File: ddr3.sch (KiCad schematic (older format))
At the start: 35 parts, among them U12 TPS51200DRC, U13 AS4C256M16D3

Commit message: DDR3 sheet edits
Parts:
- removed R51, R52: 51, Resistor_SMD:R_0402_1005Metric, symbol Device:R_Small
- removed U12: TPS51200DRC, Package_SON:VSON-10-1EP_3x3mm_P0.5mm_EP1.65x2.4mm, symbol Regulator_Linear:TPS51200DRC
- removed U13: AS4C256M16D3, Package_BGA:BGA-96_9.0x13.0mm_Layout2x3x16_P0.8mm, symbol eco_memory:AS4C256M16D3
- added R? (x2): R_51R_0402, antmicro-footprints:0402-res, symbol antmicroResistors0402:R_51R_0402
- added U? (x2): AS4C256M16D3, antmicro-footprints:BGA-96_9.0x13.0mm_Layout2x3x16_P0.8mm, symbol antmicroMemory:AS4C256M16D3
- added U?: TPS51200DRC, antmicro-footprints:VSON-10-1EP_3x3mm, symbol antmicroPMICVoltageRegulatorsDCDCSwitchingControllers:TPS51200DRC
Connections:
- net labels added: DDR3_VREF, DDR3_VTT_EN
- net labels removed: DDR3_Vref, DDR3_Vtt_EN, VO
- wire segments 334 -> 329
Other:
- note removed: "TODO:Replace 51R resistors"
- moved on the sheet: C?, R?

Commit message: Initial component placement added (to be adjusted further)
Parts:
- gave numbers to parts that had none: 35

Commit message: Update after designator unification
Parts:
- renumbered C123 to C40, C124 to C41, C125 to C42, C126 to C43, C127 to C44, C131 to C45, C132 to C46, C133 to C47, C134 to C48, C135 to C49, C137 to C50, C142 to C51, C146 to C52, C150 to C53, C154 to C54, C157 to C55, C158 to C56, C159 to C57, C160 to C58, C161 to C59, C162 to C60, C163 to C61, C164 to C62, C165 to C63, R56 to R54, R57 to R55, R58 to R56, R59 to R57, R60 to R58, R61 to R59, R62 to R60, R63 to R61, R64 to R62, U13 to U7, U14 to U8

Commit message: Add local component libraries
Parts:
- removed R61, R62: R_51R_0402, antmicro-footprints:0402-res, symbol antmicroResistors0402:R_51R_0402
- added R? (x2): R_51R_0402, antmicro-footprints:0402-res, symbol antmicroResistors0402:R_51R_0402
- C40, C41, C43, C47: footprint antmicro-footprints:0402-cap -> artix-dc-scm-footprints:0402-cap; symbol antmicroCapacitors0402:C_10u_0402 -> artix-dc-scm:C_10u_0402
- C42, C44, C45, C46, C57, C62, C63: footprint antmicro-footprints:0402-cap -> artix-dc-scm-footprints:0402-cap; symbol antmicroCapacitors0402:C_100n_0402 -> artix-dc-scm:C_100n_0402
- C48: footprint antmicro-footprints:0402-cap -> artix-dc-scm-footprints:0402-cap; symbol antmicroCapacitors0402:C_4u7_0402 -> artix-dc-scm:C_4u7_0402
- C49, C50, C51, C52, C53, C54, C55, C56, C58, C59, C60, C61: footprint antmicro-footprints:0402-cap -> artix-dc-scm-footprints:0402-cap; symbol antmicroCapacitors0402:C_470n_0402 -> artix-dc-scm:C_470n_0402
- R54, R55, R56: footprint antmicro-footprints:R_Array_Convex_8x0602 -> artix-dc-scm-footprints:R_Array_Convex_8x0602; symbol antmicroResistorNetworksArrays:8x51R_0602_array -> artix-dc-scm:8x51R_0602_array
- R57, R58, R59: footprint antmicro-footprints:0402-res -> artix-dc-scm-footprints:0402-res; symbol antmicroResistors0402:R_10k_0402 -> artix-dc-scm:R_10k_0402
- R60: footprint antmicro-footprints:0402-res -> artix-dc-scm-footprints:0402-res; symbol antmicroResistors0402:R_240R_0402 -> artix-dc-scm:R_240R_0402
- U7: footprint antmicro-footprints:BGA-96_9.0x13.0mm_Layout2x3x16_P0.8mm -> artix-dc-scm-footprints:BGA-96_9.0x13.0mm_Layout2x3x16_P0.8mm; symbol antmicroMemory:AS4C256M16D3 -> artix-dc-scm:AS4C256M16D3
- U8: footprint antmicro-footprints:VSON-10-1EP_3x3mm -> artix-dc-scm-footprints:VSON-10-1EP_3x3mm; symbol antmicroPMICVoltageRegulatorsDCDCSwitchingControllers:TPS51200DRC -> artix-dc-scm:TPS51200DRC

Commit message: Component placement done
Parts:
- R100, R99: renamed from R?; footprint antmicro-footprints:0402-res -> artix-dc-scm-footprints:0402-res; symbol antmicroResistors0402:R_51R_0402 -> artix-dc-scm:R_51R_0402
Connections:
- net DDR3_CLK+: now also R99.2; no longer R99.1
- net at C63.2, R100.1: now also R99.1; no longer R99.2
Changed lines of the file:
@@
 DDR3_VTT
 $Comp
-L antmicroResistors0402:R_51R_0402 R?
+L artix-dc-scm:R_51R_0402 R99
 U 1 1 5FDBE47E
 P 12475 8050
-F 0 "R?" V 12430 8120 60  0000 L CNN
+F 0 "R99" V 12430 8120 60  0000 L CNN
 F 1 "R_51R_0402" H 12475 7900 60  0001 C CNN
-F 2 "antmicro-footprints:0402-res" H 12675 8250 60  0001 L CNN
+F 2 "artix-dc-scm-footprints:0402-res" H 12675 8250 60  0001 L CNN
 F 3 "" H 12475 8050 50  0001 C CNN
 F 4 "YAGEO" H 12675 8450 60  0001 L CNN "Manufacturer"
@@
 F 6 "51R" V 12528 8120 50  0000 L CNN "Val"
 	1    12475 8050
-	0    1    1    0
+	0    1    -1   0
 $EndComp
 $Comp
-L antmicroResistors0402:R_51R_0402 R?
+L artix-dc-scm:R_51R_0402 R100
 U 1 1 5FDBF551
 P 12475 8450
-F 0 "R?" V 12430 8520 60  0000 L CNN
+F 0 "R100" V 12430 8520 60  0000 L CNN
 F 1 "R_51R_0402" H 12475 8300 60  0001 C CNN
-F 2 "antmicro-footprints:0402-res" H 12675 8650 60  0001 L CNN
+F 2 "artix-dc-scm-footprints:0402-res" H 12675 8650 60  0001 L CNN
 F 3 "" H 12475 8450 50  0001 C CNN
 F 4 "YAGEO" H 12675 8850 60  0001 L CNN "Manufacturer"

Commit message: Improved DDR3 related connection (WIP)
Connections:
- net DDR3_A0: now also R54.5; no longer R55.8
- net DDR3_A1: now also R55.7; no longer R55.2
- net DDR3_A10: now also R54.1; no longer R55.5
- net DDR3_A11: now also R55.8; no longer R54.8
- net DDR3_A12: now also R55.4; no longer R55.3
- net DDR3_A13: now also R54.8; no longer R54.1
- net DDR3_A14: now also R54.2; no longer R54.7
- net DDR3_A2: now also R54.6; no longer R54.4
- net DDR3_A3: now also R56.4; no longer R56.2
- net DDR3_A4: now also R55.3; no longer R55.1
- net DDR3_A5: now also R56.3; no longer R56.1
- net DDR3_A6: now also R55.5; no longer R54.5
- net DDR3_A7: now also R56.2; no longer R54.3
- net DDR3_A8: now also R55.6; no longer R54.6
- net DDR3_A9: now also R54.7; no longer R54.2
- net DDR3_BA0: now also R56.5; no longer R56.3
- net DDR3_BA1: now also R55.2; no longer R55.4
- net DDR3_BA2: now also R54.4; no longer R55.7
- net DDR3_CAS: now also R56.6; no longer R56.8
- net DDR3_CKE: now also R55.1; no longer R56.7
- net DDR3_CS: now also R56.7; no longer R56.4
- net DDR3_ODT: now also R56.8; no longer R56.6
- net DDR3_RAS: now also R56.1; no longer R56.5
- net DDR3_WE: now also R54.3; no longer R55.6
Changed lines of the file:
@@
 Wire Wire Line
 	11775 2375 11775 2700
+Text GLabel 4425 9375 0    50   UnSpc ~ 0
+DDR3_A1
+Text GLabel 4425 8975 0    50   UnSpc ~ 0
+DDR3_A4
+Text GLabel 4425 9175 0    50   UnSpc ~ 0
+DDR3_A6
+Text GLabel 4425 9275 0    50   UnSpc ~ 0
+DDR3_A8
 Text GLabel 4425 9475 0    50   UnSpc ~ 0
-DDR3_A0
+DDR3_A11
+Text GLabel 4425 9075 0    50   UnSpc ~ 0
+DDR3_A12
+Text GLabel 4425 7475 0    50   UnSpc ~ 0
+DDR3_A14
+Wire Wire Line
+	4425 9475 4625 9475
+Wire Wire Line
+	4625 8875 4425 8875
+Wire Wire Line
+	4625 7675 4425 7675
+Wire Wire Line
+	4625 10275 4425 10275
+Wire Wire Line
+	4425 8775 4625 8775
+Wire Wire Line
+	4425 10175 4625 10175
+Wire Wire Line
+	4425 7775 4625 7775
+Wire Wire Line
+	4425 7575 4625 7575
+Wire Wire Line
+	4425 7875 4625 7875
+Wire Wire Line
+	4425 7475 4625 7475
+Wire Wire Line
+	4425 9175 4625 9175
+Wire Wire Line
+	4425 8075 4625 8075
+Wire Wire Line
+	4425 8975 4625 8975
+Wire Wire Line
+	4425 7375 4625 7375
+Wire Wire Line
+	4425 7975 4625 7975
 Text GLabel 4425 8875 0    50   UnSpc ~ 0
-DDR3_A1
-Text GLabel 4425 7675 0    50   UnSpc ~ 0
-DDR3_A2
-Text GLabel 4425 10275 0    50   UnSpc ~ 0
-DDR3_A3
-Text GLabel 4425 8775 0    50   UnSpc ~ 0
-DDR3_A4
-Text GLabel 4425 10175 0    50   UnSpc ~ 0
-DDR3_A5
-Text GLabel 4425 7775 0    50   UnSpc ~ 0
-DDR3_A6
-Text GLabel 4425 7575 0    50   UnSpc ~ 0
-DDR3_A7
-Text GLabel 4425 7875 0    50   UnSpc ~ 0
-DDR3_A8
-Text GLabel 4425 7475 0    50   UnSpc ~ 0
-DDR3_A9
-Text GLabel 4425 9175 0    50   UnSpc ~ 0
-DDR3_A10
-Text GLabel 4425 8075 0    50   UnSpc ~ 0
-DDR3_A11
-Text GLabel 4425 8975 0    50   UnSpc ~ 0
-DDR3_A12
-Text GLabel 4425 7375 0    50   UnSpc ~ 0
-DDR3_A13
-Text GLabel 4425 7975 0    50   UnSpc ~ 0
-DDR3_A14
-Wire Wire Line
-	4425 9475 4625 9475
-Wire Wire Line
-	4625 8875 4425 8875
-Wire Wire Line
-	4625 7675 4425 7675
-Wire Wire Line
-	4625 10275 4425 10275
-Wire Wire Line
-	4425 8775 4625 8775
-Wire Wire Line
-	4425 10175 4625 10175
-Wire Wire Line
-	4425 7775 4625 7775
-Wire Wire Line
-	4425 7575 4625 7575
-Wire Wire Line
-	4425 7875 4625 7875
-Wire Wire Line
-	4425 7475 4625 7475
-Wire Wire Line
-	4425 9175 4625 9175
-Wire Wire Line
-	4425 8075 4625 8075
-Wire Wire Line
-	4425 8975 4625 8975
-Wire Wire Line
-	4425 7375 4625 7375
-Wire Wire Line
-	4425 7975 4625 7975
-Text GLabel 4425 10375 0    50   UnSpc ~ 0
-DDR3_BA0
-Text GLabel 4425 9075 0    50   UnSpc ~ 0
 DDR3_BA1
-Text GLabel 4425 9375 0    50   UnSpc ~ 0
-DDR3_BA2
 Wire Wire Line
 	4425 10375 4625 10375
@@
 Wire Wire Line
 	4425 9375 4625 9375
-Text GLabel 4425 10575 0    50   UnSpc ~ 0
-DDR3_RAS
-Text GLabel 4425 10875 0    50   UnSpc ~ 0
-DDR3_CAS
 Wire Wire Line
 	4425 10875 4625 10875
 Wire Wire Line
 	4625 10575 4425 10575
-Text GLabel 4425 9275 0    50   UnSpc ~ 0
-DDR3_WE
-Text GLabel 4425 10475 0    50   UnSpc ~ 0
-DDR3_CS
 Wire Wire Line
 	4625 9275 4425 9275
 Wire Wire Line
 	4425 10475 4625 10475
-Text GLabel 4425 10775 0    50   UnSpc ~ 0
-DDR3_CKE
-Text GLabel 4425 10675 0    50   UnSpc ~ 0
-DDR3_ODT
 Wire Wire Line
 	4425 10675 4625 10675
@@
 	0    1    1    0
 $EndComp
+Text GLabel 4425 10875 0    50   UnSpc ~ 0
+DDR3_ODT
+Text GLabel 4425 8775 0    50   UnSpc ~ 0
+DDR3_CKE
+Text GLabel 4425 10775 0    50   UnSpc ~ 0
+DDR3_CS
+Text GLabel 4425 10675 0    50   UnSpc ~ 0
+DDR3_CAS
+Text GLabel 4425 10175 0    50   UnSpc ~ 0
+DDR3_RAS
+Text GLabel 4425 10575 0    50   UnSpc ~ 0
+DDR3_BA0
+Text GLabel 4425 10475 0    50   UnSpc ~ 0
+DDR3_A3
+Text GLabel 4425 7575 0    50   UnSpc ~ 0
+DDR3_WE
+Text GLabel 4425 7675 0    50   UnSpc ~ 0
+DDR3_BA2
+Text GLabel 4425 10275 0    50   UnSpc ~ 0
+DDR3_A7
+Text GLabel 4425 7875 0    50   UnSpc ~ 0
+DDR3_A2
+Text GLabel 4425 7775 0    50   UnSpc ~ 0
+DDR3_A0
+Text GLabel 4425 10375 0    50   UnSpc ~ 0
+DDR3_A5
+Text GLabel 4425 7375 0    50   UnSpc ~ 0
+DDR3_A10
+Text GLabel 4425 8075 0    50   UnSpc ~ 0
+DDR3_A13
+Text GLabel 4425 7975 0    50   UnSpc ~ 0
+DDR3_A9
 $EndSCHEMATC

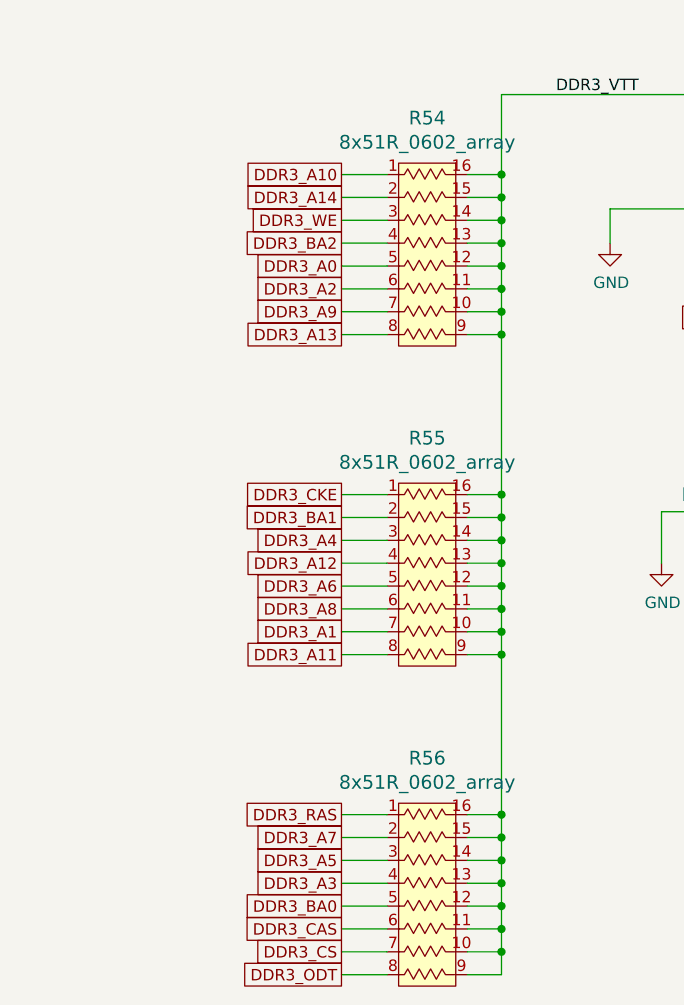
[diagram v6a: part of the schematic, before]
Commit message: Improved DDR3 to FPGA connections (WIP)
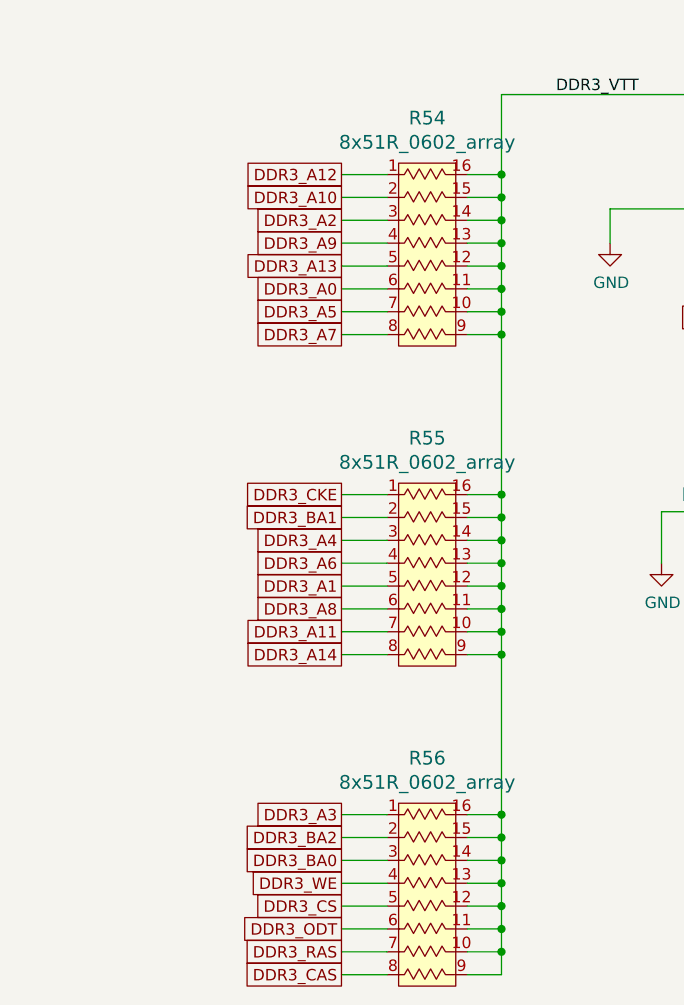
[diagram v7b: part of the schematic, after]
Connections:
- net DDR3_A0: now also R54.6; no longer R54.5
- net DDR3_A1: now also R55.5; no longer R55.7
- net DDR3_A10: now also R54.2; no longer R54.1
- net DDR3_A11: now also R55.7; no longer R55.8
- net DDR3_A12: now also R54.1; no longer R55.4
- net DDR3_A13: now also R54.5; no longer R54.8
- net DDR3_A14: now also R55.8; no longer R54.2
- net DDR3_A2: now also R54.3; no longer R54.6
- net DDR3_A3: now also R56.1; no longer R56.4
- net DDR3_A5: now also R54.7; no longer R56.3
- net DDR3_A6: now also R55.4; no longer R55.5
- net DDR3_A7: now also R54.8; no longer R56.2
- net DDR3_A9: now also R54.4; no longer R54.7
- net DDR3_BA0: now also R56.3; no longer R56.5
- net DDR3_BA2: now also R56.2; no longer R54.4
- net DDR3_CAS: now also R56.8; no longer R56.6
- net DDR3_CS: now also R56.5; no longer R56.7
- net DDR3_ODT: now also R56.6; no longer R56.8
- net DDR3_RAS: now also R56.7; no longer R56.1
- net DDR3_WE: now also R56.4; no longer R54.3
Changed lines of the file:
@@
 Wire Wire Line
 	11775 2375 11775 2700
-Text GLabel 4425 9375 0    50   UnSpc ~ 0
+Text GLabel 4425 9175 0    50   UnSpc ~ 0
 DDR3_A1
 Text GLabel 4425 8975 0    50   UnSpc ~ 0
 DDR3_A4
-Text GLabel 4425 9175 0    50   UnSpc ~ 0
+Text GLabel 4425 9075 0    50   UnSpc ~ 0
 DDR3_A6
 Text GLabel 4425 9275 0    50   UnSpc ~ 0
 DDR3_A8
+Text GLabel 4425 9375 0    50   UnSpc ~ 0
+DDR3_A11
+Text GLabel 4425 7375 0    50   UnSpc ~ 0
+DDR3_A12
 Text GLabel 4425 9475 0    50   UnSpc ~ 0
-DDR3_A11
-Text GLabel 4425 9075 0    50   UnSpc ~ 0
-DDR3_A12
-Text GLabel 4425 7475 0    50   UnSpc ~ 0
 DDR3_A14
 Wire Wire Line
@@
 	0    1    1    0
 $EndComp
-Text GLabel 4425 10875 0    50   UnSpc ~ 0
+Text GLabel 4425 10675 0    50   UnSpc ~ 0
 DDR3_ODT
 Text GLabel 4425 8775 0    50   UnSpc ~ 0
 DDR3_CKE
+Text GLabel 4425 10575 0    50   UnSpc ~ 0
+DDR3_CS
+Text GLabel 4425 10875 0    50   UnSpc ~ 0
+DDR3_CAS
 Text GLabel 4425 10775 0    50   UnSpc ~ 0
-DDR3_CS
-Text GLabel 4425 10675 0    50   UnSpc ~ 0
-DDR3_CAS
+DDR3_RAS
+Text GLabel 4425 10375 0    50   UnSpc ~ 0
+DDR3_BA0
 Text GLabel 4425 10175 0    50   UnSpc ~ 0
-DDR3_RAS
-Text GLabel 4425 10575 0    50   UnSpc ~ 0
-DDR3_BA0
+DDR3_A3
 Text GLabel 4425 10475 0    50   UnSpc ~ 0
-DDR3_A3
+DDR3_WE
+Text GLabel 4425 10275 0    50   UnSpc ~ 0
+DDR3_BA2
+Text GLabel 4425 8075 0    50   UnSpc ~ 0
+DDR3_A7
 Text GLabel 4425 7575 0    50   UnSpc ~ 0
-DDR3_WE
+DDR3_A2
+Text GLabel 4425 7875 0    50   UnSpc ~ 0
+DDR3_A0
+Text GLabel 4425 7975 0    50   UnSpc ~ 0
+DDR3_A5
+Text GLabel 4425 7475 0    50   UnSpc ~ 0
+DDR3_A10
+Text GLabel 4425 7775 0    50   UnSpc ~ 0
+DDR3_A13
 Text GLabel 4425 7675 0    50   UnSpc ~ 0
-DDR3_BA2
-Text GLabel 4425 10275 0    50   UnSpc ~ 0
-DDR3_A7
-Text GLabel 4425 7875 0    50   UnSpc ~ 0
-DDR3_A2
-Text GLabel 4425 7775 0    50   UnSpc ~ 0
-DDR3_A0
-Text GLabel 4425 10375 0    50   UnSpc ~ 0
-DDR3_A5
-Text GLabel 4425 7375 0    50   UnSpc ~ 0
-DDR3_A10
-Text GLabel 4425 8075 0    50   UnSpc ~ 0
-DDR3_A13
-Text GLabel 4425 7975 0    50   UnSpc ~ 0
 DDR3_A9
 $EndSCHEMATC
